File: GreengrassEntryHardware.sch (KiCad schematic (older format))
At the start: 31 parts, among them J1 USB_B_Micro, J2 GPIOBreakout, J3 Raspberry_Pi_2_3, J4 AutomaticSlidingDoor, J5 MFRC-522, U1 CH340G, Y1 12MHZ

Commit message: Radical redesign using nets, mini spox, larger board, traces on underside
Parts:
- added J6: DoorEnable, GreengrassEntryHardware:Molex-MiniSpox-22057025-02-Horizontal, symbol Connector_Generic:Conn_01x02
- added J8: FEEDBACK, GreengrassEntryHardware:Molex-MiniSpox-22057025-03-Horizontal, symbol Connector_Generic:Conn_01x03
- added R20, R21, R23: 27, Resistor_SMD:R_0805_2012Metric_Pad1.15x1.40mm_HandSolder, symbol Device:R_US
- added R22: 10k, Resistor_SMD:R_0805_2012Metric_Pad1.15x1.40mm_HandSolder, symbol Device:R_US
- J1: footprint GreengrassEntryHardware:MicroUSB -> GreengrassEntryHardware:USB_Micro-B_Molex-105017-0001
- J4: footprint GreengrassEntryHardware:Molex_SPOX_5267-06A_1x06_P2.50mm_Horizontal -> GreengrassEntryHardware:Molex-MiniSpox-22057xx5-08-Horizontal; symbol Connector_Generic:Conn_01x06 -> Connector_Generic:Conn_01x08
- J5: footprint GreengrassEntryHardware:Molex_Micro-Fit_3.0_43045-1000_2x05_P3.00mm_Horizontal -> GreengrassEntryHardware:Molex-MiniSpox-22057xx5-08-Horizontal; symbol Connector_Generic:Conn_01x10 -> Connector_Generic:Conn_01x08
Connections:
- net AUTO: now also J3.31 (GCLK2/GPIO6), R15.2; no longer J4.4 (Pin_4), R8.1
- net AUTO_OUT: now also J3.29 (GCLK1/GPIO5), R9.2; no longer J4.5 (Pin_5), R15.1
- net CLOSED: now also J3.27 (ID_SD/GPIO0), R21.2; no longer J4.6 (Pin_6), R9.1
- net EXIT: now also J3.36 (GPIO16), R14.2; no longer J4.2 (Pin_2), R7.1
- net GNDD: now also J4.8 (Pin_8), J6.2 (Pin_2), J8.1 (Pin_1), R22.2
- net GPIO17: now also J3.11 (GPIO17), R4.1; no longer J2.3 (Pin_3), R4.2
- net GPIO22: now also J3.15 (GPIO22), R6.1; no longer J2.5 (Pin_5), R6.2
- net GPIO27: now also J3.13 (GPIO27), R5.1; no longer J2.4 (Pin_4), R5.2
- net GPIO4: now also J3.7 (GCLK0/GPIO4), R3.1; no longer J2.2 (Pin_2), R3.2
- net OPEN: now also J3.33 (PWM1/GPIO13), R8.2; no longer J4.3 (Pin_3), R14.1
- net FEEDBACK-BUZZER: now reaches J3.16 (GPIO23)
- net FEEDBACK-BUZZER: now also R13.2; no longer R18.2
- net FEEDBACK-LED: now reaches J3.18 (GPIO24)
- net FEEDBACK-LED: now also R18.2; no longer R13.2
- net RFID-MOSI: now reaches J3.19 (MOSI0/GPIO10), R11.2
- net RFID-MISO: now reaches J3.21 (MISO0/GPIO9), R16.2
- net RFID-RST: now reaches J3.22 (GPIO25), R12.2
- net RFID-SCK: now reaches J3.23 (SCLK0/GPIO11), R17.2
- net RFID-CS: now reaches J3.24 (~CE0~/GPIO8), R10.2
- net ENABLE: now reaches J3.28 (ID_SC/GPIO1)
- net ENABLE: now also R20.2, R22.1
- net ACTIVATE: now reaches J3.37 (GPIO26), R7.2
- net 3.3V: no longer names the net of J3.17 (3V3), J5.8 (Pin_8)
- net BUZZER: no longer names the net of R18.1
- net BUZZER: now also J8.3 (Pin_3); no longer J5.10 (Pin_10)
- net IRQ: no longer names the net of J5.5 (Pin_5)
- net IRQ: now also R23.1
- net LED: no longer names the net of R13.1
- net LED: now also J8.2 (Pin_2); no longer J5.9 (Pin_9)
- net MISO: no longer names the net of J5.4 (Pin_4), R16.1
- net MOSI: no longer names the net of J5.3 (Pin_3), R11.1
- net RST: no longer names the net of J5.7 (Pin_7), R12.1
- net SCK: no longer names the net of J5.2 (Pin_2), R17.1
- net SDA-CS: no longer names the net of J5.1 (Pin_1), R10.1
- new net: J4.2 (Pin_2), R7.1
- new net: J4.3 (Pin_3), R14.1
- new net: J4.4 (Pin_4), R8.1
- new net: J4.5 (Pin_5), R15.1
- new net: J4.6 (Pin_6), R9.1
- new net: J4.7 (Pin_7), R21.1
- new net: J2.2 (Pin_2), R3.2
- new net: J2.3 (Pin_3), R4.2
- new net: J2.4 (Pin_4), R5.2
- new net: J2.5 (Pin_5), R6.2
- new net: J6.1 (Pin_1), R20.1
- new net RFID-IRQ: R23.2
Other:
- moved on the sheet: C1, C2, C3, C4, D1, J1, J2, J3, R1, R10, R11, R12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

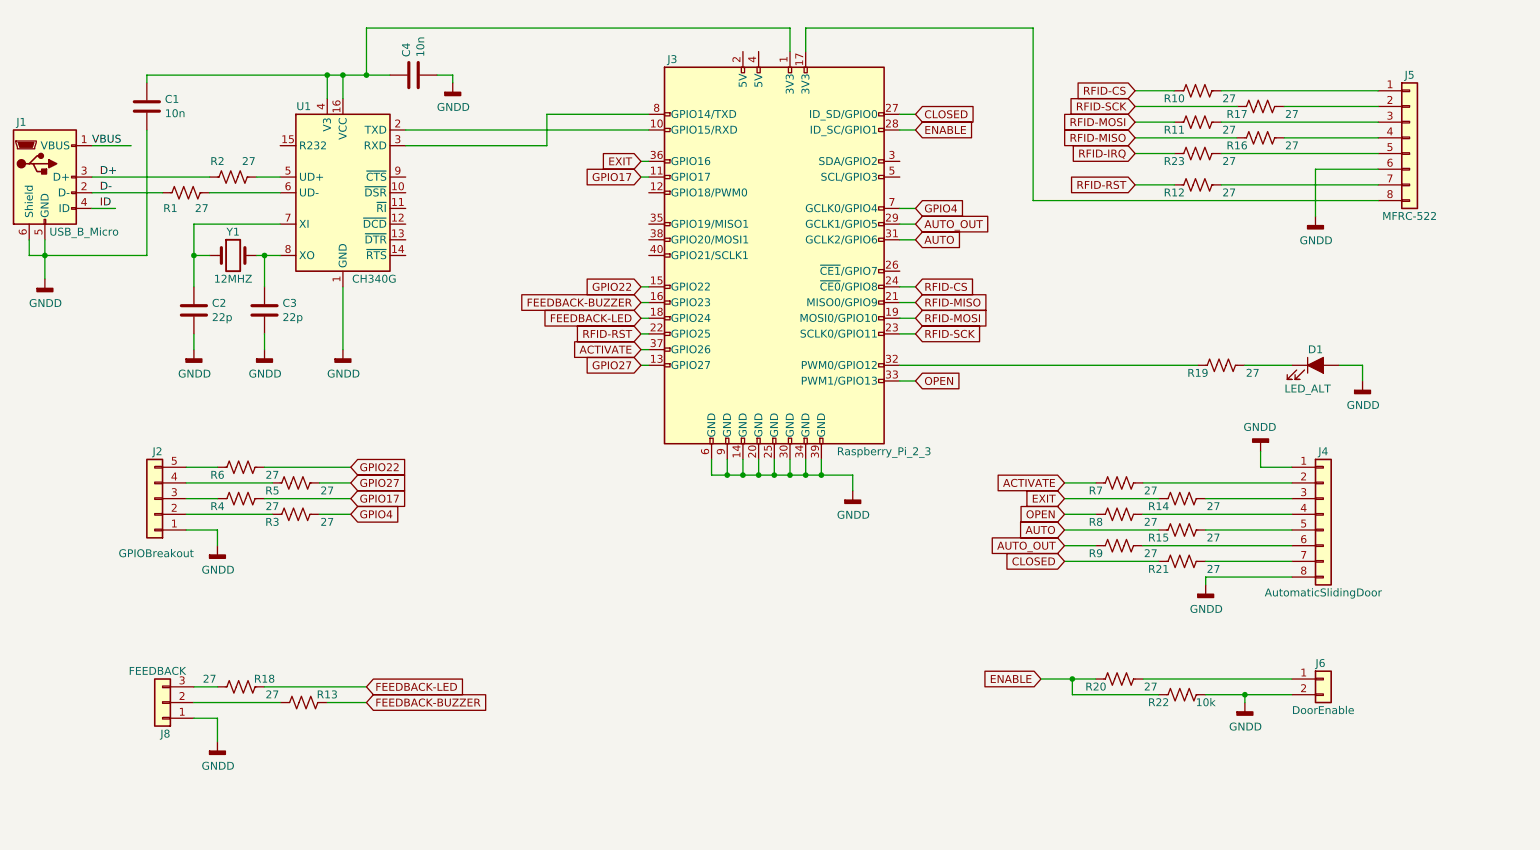
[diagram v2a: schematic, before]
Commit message: Push 5v to the relays
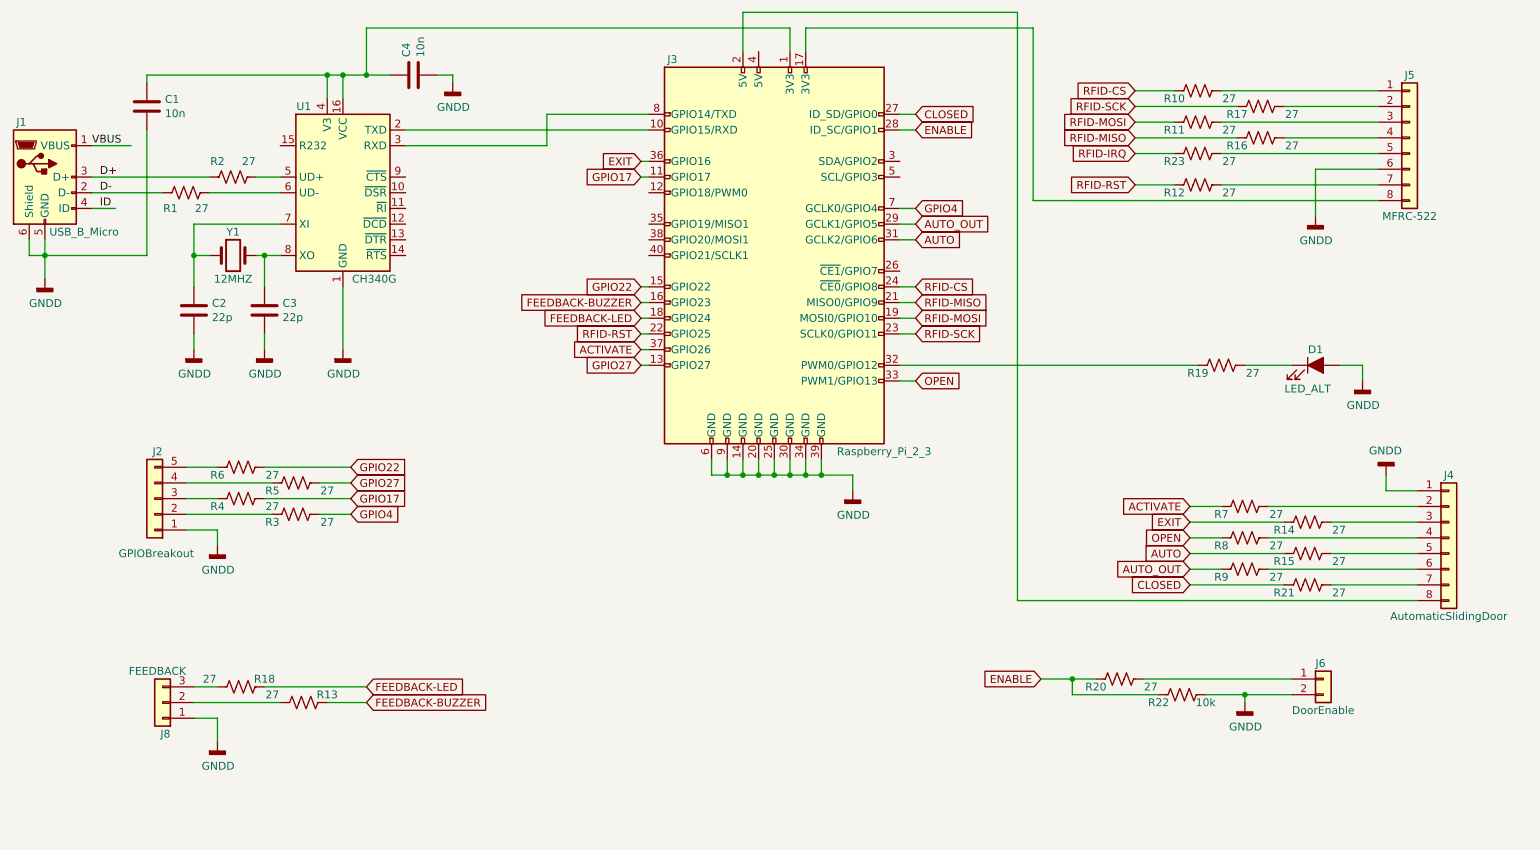
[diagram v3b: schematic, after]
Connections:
- net GNDD: no longer J4.8 (Pin_8)
- net at J3.2 (5V): now also J4.8 (Pin_8)
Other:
- moved on the sheet: J4, R14, R15, R21, R7, R8, R9
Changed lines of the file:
@@
 L Connector_Generic:Conn_01x08 J4
 U 1 1 5D3C1839
-P 9400 4650
-F 0 "J4" H 9400 5050 50  0000 C CNN
-F 1 "AutomaticSlidingDoor" H 9400 4150 50  0000 C CNN
-F 2 "GreengrassEntryHardware:Molex-MiniSpox-22057xx5-08-Horizontal" H 9400 4650 50  0001 C CNN
-F 3 "~" H 9400 4650 50  0001 C CNN
-	1    9400 4650
+P 10200 4800
+F 0 "J4" H 10200 5200 50  0000 C CNN
+F 1 "AutomaticSlidingDoor" H 10200 4300 50  0000 C CNN
+F 2 "GreengrassEntryHardware:Molex-MiniSpox-22057xx5-08-Horizontal" H 10200 4800 50  0001 C CNN
+F 3 "~" H 10200 4800 50  0001 C CNN
+	1    10200 4800
 	1    0    0    -1
 $EndComp
@@
 L Device:R_US R7
 U 1 1 5D49F22C
-P 8100 4450
-F 0 "R7" V 8150 4300 50  0000 C CNN
-F 1 "27" V 8150 4650 50  0000 C CNN
-F 2 "Resistor_SMD:R_0805_2012Metric_Pad1.15x1.40mm_HandSolder" V 8140 4440 50  0001 C CNN
-F 3 "~" H 8100 4450 50  0001 C CNN
-	1    8100 4450
+P 8900 4600
+F 0 "R7" V 8950 4450 50  0000 C CNN
+F 1 "27" V 8950 4800 50  0000 C CNN
+F 2 "Resistor_SMD:R_0805_2012Metric_Pad1.15x1.40mm_HandSolder" V 8940 4590 50  0001 C CNN
+F 3 "~" H 8900 4600 50  0001 C CNN
+	1    8900 4600
 	0    1    1    0
 $EndComp
@@
 L Device:R_US R8
 U 1 1 5D49F7A2
-P 8100 4650
-F 0 "R8" V 8150 4500 50  0000 C CNN
-F 1 "27" V 8150 4850 50  0000 C CNN
-F 2 "Resistor_SMD:R_0805_2012Metric_Pad1.15x1.40mm_HandSolder" V 8140 4640 50  0001 C CNN
-F 3 "~" H 8100 4650 50  0001 C CNN
-	1    8100 4650
+P 8900 4800
+F 0 "R8" V 8950 4650 50  0000 C CNN
+F 1 "27" V 8950 5000 50  0000 C CNN
+F 2 "Resistor_SMD:R_0805_2012Metric_Pad1.15x1.40mm_HandSolder" V 8940 4790 50  0001 C CNN
+F 3 "~" H 8900 4800 50  0001 C CNN
+	1    8900 4800
 	0    1    1    0
 $EndComp
@@
 L Device:R_US R9
 U 1 1 5D49FDC6
-P 8100 4850
-F 0 "R9" V 8150 4700 50  0000 C CNN
-F 1 "27" V 8150 5050 50  0000 C CNN
-F 2 "Resistor_SMD:R_0805_2012Metric_Pad1.15x1.40mm_HandSolder" V 8140 4840 50  0001 C CNN
-F 3 "~" H 8100 4850 50  0001 C CNN
-	1    8100 4850
+P 8900 5000
+F 0 "R9" V 8950 4850 50  0000 C CNN
+F 1 "27" V 8950 5200 50  0000 C CNN
+F 2 "Resistor_SMD:R_0805_2012Metric_Pad1.15x1.40mm_HandSolder" V 8940 4990 50  0001 C CNN
+F 3 "~" H 8900 5000 50  0001 C CNN
+	1    8900 5000
 	0    1    1    0
 $EndComp
@@
 L Device:R_US R14
 U 1 1 5D4A0302
-P 8500 4550
-F 0 "R14" V 8550 4400 50  0000 C CNN
-F 1 "27" V 8550 4750 50  0000 C CNN
-F 2 "Resistor_SMD:R_0805_2012Metric_Pad1.15x1.40mm_HandSolder" V 8540 4540 50  0001 C CNN
-F 3 "~" H 8500 4550 50  0001 C CNN
-	1    8500 4550
+P 9300 4700
+F 0 "R14" V 9350 4550 50  0000 C CNN
+F 1 "27" V 9350 4900 50  0000 C CNN
+F 2 "Resistor_SMD:R_0805_2012Metric_Pad1.15x1.40mm_HandSolder" V 9340 4690 50  0001 C CNN
+F 3 "~" H 9300 4700 50  0001 C CNN
+	1    9300 4700
 	0    1    1    0
 $EndComp
@@
 L Device:R_US R15
 U 1 1 5D4A157F
-P 8500 4750
-F 0 "R15" V 8550 4600 50  0000 C CNN
-F 1 "27" V 8550 4950 50  0000 C CNN
-F 2 "Resistor_SMD:R_0805_2012Metric_Pad1.15x1.40mm_HandSolder" V 8540 4740 50  0001 C CNN
-F 3 "~" H 8500 4750 50  0001 C CNN
-	1    8500 4750
+P 9300 4900
+F 0 "R15" V 9350 4750 50  0000 C CNN
+F 1 "27" V 9350 5100 50  0000 C CNN
+F 2 "Resistor_SMD:R_0805_2012Metric_Pad1.15x1.40mm_HandSolder" V 9340 4890 50  0001 C CNN
+F 3 "~" H 9300 4900 50  0001 C CNN
+	1    9300 4900
 	0    1    1    0
 $EndComp
@@
 	8750 2550 9750 2550
 Wire Wire Line
-	8250 4450 9200 4450
-Wire Wire Line
-	8650 4550 9200 4550
-Wire Wire Line
-	8250 4650 9200 4650
-Wire Wire Line
-	8650 4750 9200 4750
-Wire Wire Line
-	8250 4850 9200 4850
+	9050 4600 10000 4600
+Wire Wire Line
+	9450 4700 10000 4700
+Wire Wire Line
+	9050 4800 10000 4800
+Wire Wire Line
+	9450 4900 10000 4900
+Wire Wire Line
+	9050 5000 10000 5000
 Wire Wire Line
 	1550 2700 1700 2700
@@
 L Device:R_US R21
 U 1 1 5D4DF05D
-P 8500 4950
-F 0 "R21" V 8550 4800 50  0000 C CNN
-F 1 "27" V 8550 5150 50  0000 C CNN
-F 2 "Resistor_SMD:R_0805_2012Metric_Pad1.15x1.40mm_HandSolder" V 8540 4940 50  0001 C CNN
-F 3 "~" H 8500 4950 50  0001 C CNN
-	1    8500 4950
-	0    1    1    0
-$EndComp
-Wire Wire Line
-	9200 4950 8650 4950
+P 9300 5100
+F 0 "R21" V 9350 4950 50  0000 C CNN
+F 1 "27" V 9350 5300 50  0000 C CNN
+F 2 "Resistor_SMD:R_0805_2012Metric_Pad1.15x1.40mm_HandSolder" V 9340 5090 50  0001 C CNN
+F 3 "~" H 9300 5100 50  0001 C CNN
+	1    9300 5100
+	0    1    1    0
+$EndComp
+Wire Wire Line
+	10000 5100 9450 5100
 $Comp
 L Device:R_US R20
@@
 $EndComp
 $Comp
-L power:GNDD #PWR0102
-U 1 1 5D7289D2
-P 8650 5100
-F 0 "#PWR0102" H 8650 4850 50  0001 C CNN
-F 1 "GNDD" H 8654 4945 50  0000 C CNN
-F 2 "" H 8650 5100 50  0001 C CNN
-F 3 "" H 8650 5100 50  0001 C CNN
-	1    8650 5100
-	1    0    0    -1
-$EndComp
-$Comp
 L power:GNDD #PWR0103
 U 1 1 5D781BC2
-P 9000 4250
-F 0 "#PWR0103" H 9000 4000 50  0001 C CNN
-F 1 "GNDD" H 9004 4095 50  0000 C CNN
-F 2 "" H 9000 4250 50  0001 C CNN
-F 3 "" H 9000 4250 50  0001 C CNN
-	1    9000 4250
+P 9800 4400
+F 0 "#PWR0103" H 9800 4150 50  0001 C CNN
+F 1 "GNDD" H 9804 4245 50  0000 C CNN
+F 2 "" H 9800 4400 50  0001 C CNN
+F 3 "" H 9800 4400 50  0001 C CNN
+	1    9800 4400
 	-1   0    0    1
 $EndComp
 Wire Wire Line
-	9000 4250 9000 4350
-Wire Wire Line
-	9000 4350 9200 4350
+	9800 4400 9800 4500
+Wire Wire Line
+	9800 4500 10000 4500
 $Comp
 L power:GNDD #PWR0104
@@
 	1    0    0    -1
 $EndComp
-Wire Wire Line
-	8650 5050 8650 5100
-Wire Wire Line
-	8650 5050 9200 5050
 $Comp
 L power:GNDD #PWR0106
@@
 $EndComp
 Wire Wire Line
-	6000 1550 6000 1700
-Wire Wire Line
 	3450 1850 3300 1850
 Connection ~ 3300 1850
@@
 	3750 1850 3850 1850
 Wire Wire Line
-	3300 1550 6000 1550
-Wire Wire Line
-	3300 1550 3300 1850
-Wire Wire Line
 	2650 3000 2750 3000
 Wire Wire Line
@@
 Wire Wire Line
 	3550 2300 4450 2300
-Wire Wire Line
-	6100 1550 6100 1700
 Text GLabel 3200 4650 2    50   Input ~ 0
 GPIO4
@@
 Wire Wire Line
 	3000 4650 3200 4650
-Text GLabel 7750 4450 0    50   Input ~ 0
+Text GLabel 8550 4600 0    50   Input ~ 0
 ACTIVATE
 Wire Wire Line
-	7750 4450 7950 4450
+	8550 4600 8750 4600
 Text GLabel 5050 3600 0    50   Input ~ 0
 ACTIVATE
 Wire Wire Line
 	5050 3600 5100 3600
-Text GLabel 7750 4550 0    50   Input ~ 0
+Text GLabel 8550 4700 0    50   Input ~ 0
 EXIT
 Wire Wire Line
-	7750 4550 8350 4550
+	8550 4700 9150 4700
 Text GLabel 5050 2400 0    50   Input ~ 0
 EXIT
 Wire Wire Line
 	5050 2400 5100 2400
-Text GLabel 7750 4650 0    50   Input ~ 0
+Text GLabel 8550 4800 0    50   Input ~ 0
 OPEN
 Wire Wire Line
-	7750 4650 7950 4650
+	8550 4800 8750 4800
 Text GLabel 6800 3800 2    50   Input ~ 0
 OPEN
-Text GLabel 7750 4750 0    50   Input ~ 0
+Text GLabel 8550 4900 0    50   Input ~ 0
 AUTO
 Wire Wire Line
-	7750 4750 8350 4750
+	8550 4900 9150 4900
 Text GLabel 6800 2900 2    50   Input ~ 0
 AUTO
 Wire Wire Line
 	6700 2900 6800 2900
-Text GLabel 7750 4850 0    50   Input ~ 0
+Text GLabel 8550 5000 0    50   Input ~ 0
 AUTO_OUT
 Wire Wire Line
-	7750 4850 7950 4850
+	8550 5000 8750 5000
 Text GLabel 6800 2800 2    50   Input ~ 0
 AUTO_OUT
 Wire Wire Line
 	6700 2800 6800 2800
-Text GLabel 7750 4950 0    50   Input ~ 0
+Text GLabel 8550 5100 0    50   Input ~ 0
 CLOSED
 Wire Wire Line
-	7750 4950 8350 4950
+	8550 5100 9150 5100
 Text GLabel 6800 2100 2    50   Input ~ 0
 CLOSED
@@
 	3300 5750 2650 5750
 Wire Wire Line
-	6100 1550 7550 1550
-Wire Wire Line
 	7550 2650 9750 2650
 Text GLabel 5050 3300 0    50   Input ~ 0
@@
 Wire Wire Line
 	6700 3700 8600 3700
-Wire Wire Line
-	7550 1550 7550 2650
 Wire Wire Line
 	6700 3800 6800 3800
@@
 Wire Wire Line
 	2350 5950 2350 6100
+Wire Wire Line
+	7450 5200 7450 1450
+Wire Wire Line
+	7450 1450 5700 1450
+Wire Wire Line
+	5700 1450 5700 1700
+Wire Wire Line
+	7450 5200 10000 5200
+Wire Wire Line
+	3300 1550 3300 1850
+Wire Wire Line
+	6000 1550 6000 1700
+Wire Wire Line
+	3300 1550 6000 1550
+Wire Wire Line
+	7550 1550 7550 2650
+Wire Wire Line
+	6100 1550 6100 1700
+Wire Wire Line
+	6100 1550 7550 1550
 $EndSCHEMATC
